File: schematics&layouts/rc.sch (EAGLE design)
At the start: 17 parts, among them IC1 L293D, IC2 L293D, Q1 16MHz, U1 ATMEGA328P-PU

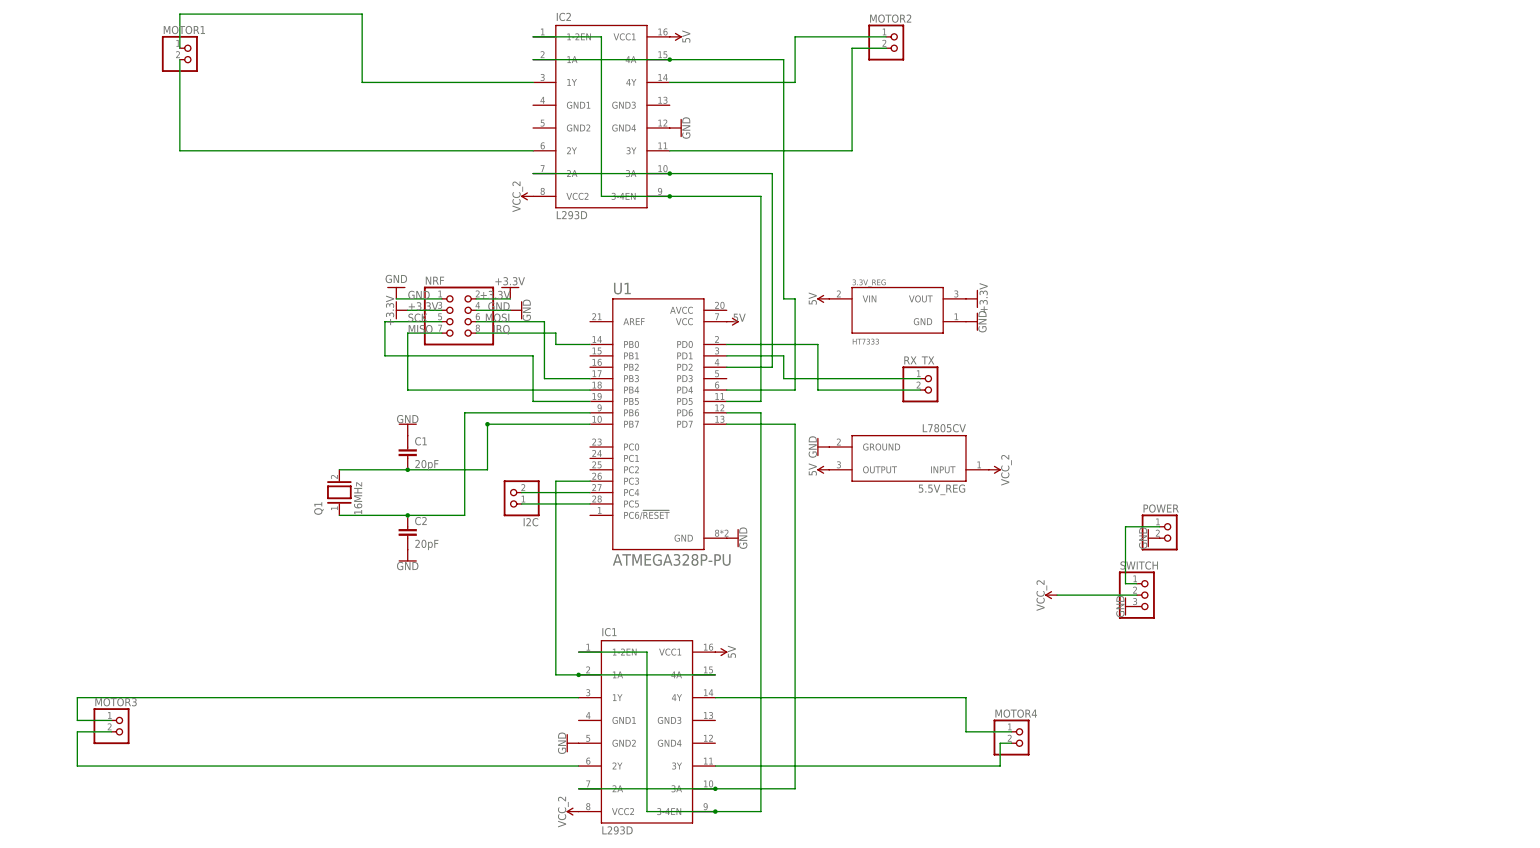
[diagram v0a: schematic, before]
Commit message: update schematic
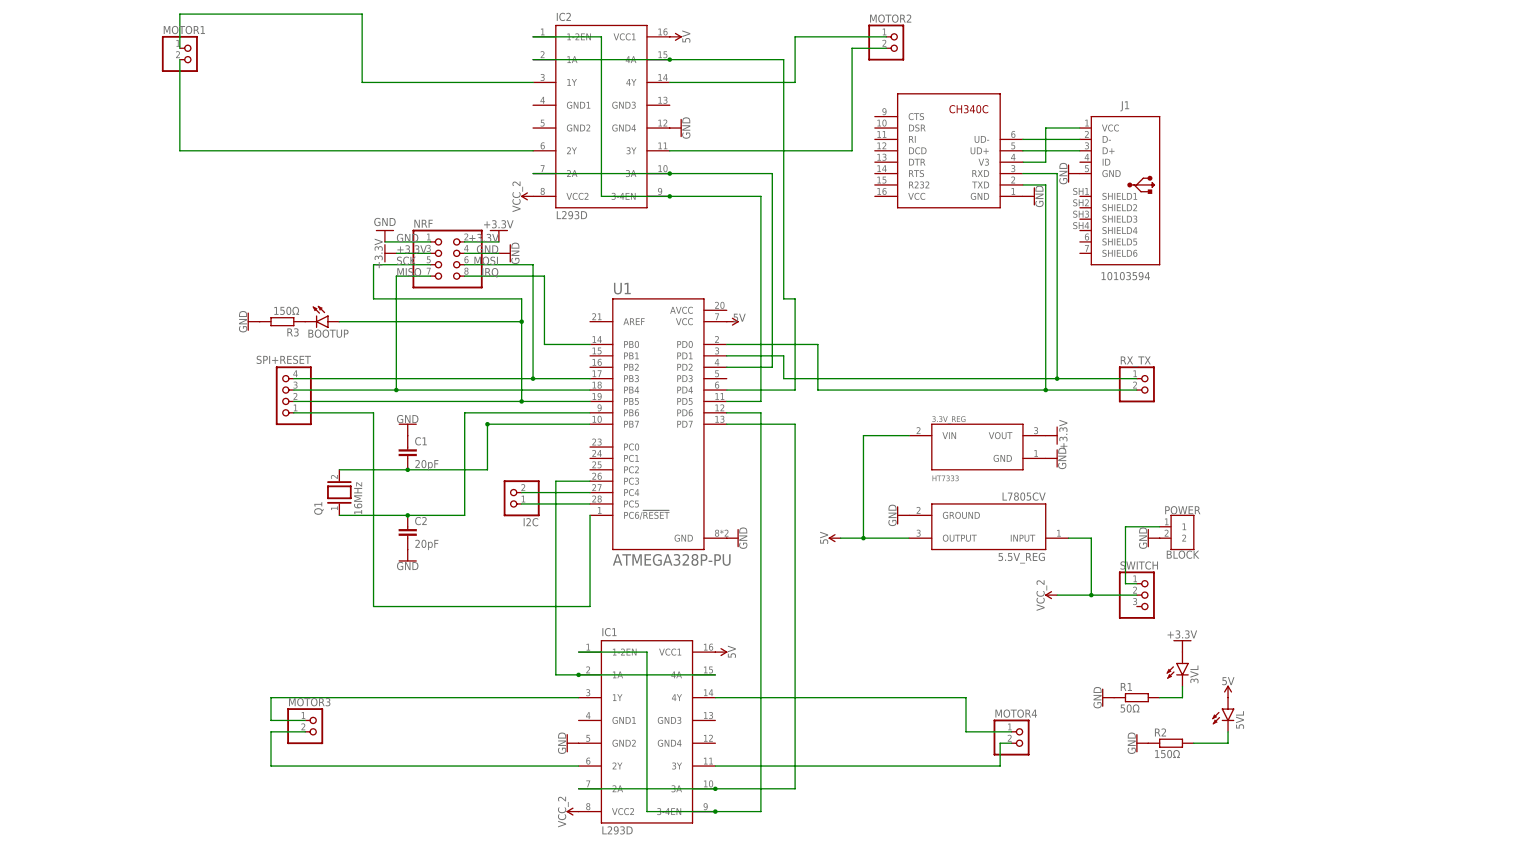
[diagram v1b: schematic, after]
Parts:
- added 3VL, 5VL, BOOTUP: (no value), led:LED5MM
- added J1: 10103594, Connector_USB:10103594
- added JP1: SPI+RESET, pinhead:PINHD-1X4
- added R1: 50Ω, rcl:R-EU_0204/7
- added R2, R3: 150Ω, rcl:R-EU_0204/7
- added U$1: CH340C, CH340C:CH340C
- POWER: value (none) -> BLOCK; device pinhead:PINHD-1X2 -> Connector:2828XX-2282834-2
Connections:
- new net N$22: 5VL.C, R2.2
- new net N$23: 3VL.C, R1.2
- new net N$24: J1.D-, U$1.UD-
- new net N$25: JP1.1, U1.PC6/!RESET
- new net N$26: J1.D+, U$1.UD+
- new net N$29: J1.VCC, U$1.V3
- net +3.3V: now also 3VL.A
- net 5V: now also 5VL.A
- net GND: now also BOOTUP.C, J1.GND, R1.1, R2.1, R3.1, R3.2, U$1.GND; no longer SWITCH.3
- net MISO: now also JP1.3
- net MOSI: now also JP1.4
- net N$18: now also U$1.TXD
- net N$2: now also U$1.RXD
- net SCK: now also BOOTUP.A, JP1.2
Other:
- moved on the sheet: 3.3V_REG, 5.5V_REG, MOTOR3, NRF, POWER, RX_TX

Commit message: updated schm
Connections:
- net N$7: now also MOTOR1.2; no longer MOTOR1.1
- net N$8: now also MOTOR1.1; no longer MOTOR1.2
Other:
- moved on the sheet: J1, MOTOR1, MOTOR2, RX_TX
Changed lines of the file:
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@@
 <attribute name="VALUE" x="56.134" y="111.76" size="1.778" layer="96" font="vector" rot="R90" align="top-center"/>
 </instance>
-<instance part="RX_TX" gate="G$1" x="198.12" y="81.28" smashed="yes">
-<attribute name="NAME" x="191.77" y="86.995" size="1.778" layer="95"/>
-<attribute name="VALUE" x="191.77" y="76.2" size="1.778" layer="96"/>
+<instance part="RX_TX" gate="G$1" x="226.06" y="91.44" smashed="yes" rot="R180">
+<attribute name="NAME" x="232.41" y="98.425" size="1.778" layer="95" rot="R180"/>
+<attribute name="VALUE" x="232.41" y="96.52" size="1.778" layer="96" rot="R180"/>
 </instance>
 <instance part="I2C" gate="G$1" x="55.88" y="58.42" smashed="yes" rot="R180">
@@
 <attribute name="VALUE" x="106.934" y="48.26" size="1.778" layer="96" font="vector" rot="R90" align="top-center"/>
 </instance>
-<instance part="MOTOR2" gate="G$1" x="142.24" y="157.48" smashed="yes">
-<attribute name="NAME" x="135.89" y="163.195" size="1.778" layer="95"/>
-<attribute name="VALUE" x="135.89" y="152.4" size="1.778" layer="96"/>
-</instance>
-<instance part="MOTOR1" gate="G$1" x="-15.24" y="154.94" smashed="yes">
-<attribute name="NAME" x="-21.59" y="160.655" size="1.778" layer="95"/>
-<attribute name="VALUE" x="-21.59" y="149.86" size="1.778" layer="96"/>
+<instance part="MOTOR2" gate="G$1" x="152.4" y="142.24" smashed="yes">
+<attribute name="NAME" x="146.05" y="147.955" size="1.778" layer="95"/>
+<attribute name="VALUE" x="146.05" y="137.16" size="1.778" layer="96"/>
+</instance>
+<instance part="MOTOR1" gate="G$1" x="-12.7" y="144.78" smashed="yes" rot="R180">
+<attribute name="NAME" x="-6.35" y="139.065" size="1.778" layer="95" rot="R180"/>
+<attribute name="VALUE" x="-6.35" y="149.86" size="1.778" layer="96" rot="R180"/>
 </instance>
 <instance part="SUPPLY5" gate="G$1" x="91.44" y="160.02" smashed="yes" rot="R270">
@@
 <attribute name="VALUE" x="-2.794" y="96.52" size="1.778" layer="96" font="vector" rot="R270" align="top-center"/>
 </instance>
-<instance part="J1" gate="G$1" x="193.04" y="127" smashed="yes">
-<attribute name="NAME" x="193.04" y="144.78" size="1.778" layer="95" align="center"/>
-<attribute name="VALUE" x="193.04" y="106.68" size="1.778" layer="96" align="center"/>
-</instance>
-<instance part="GND15" gate="1" x="172.72" y="124.46" smashed="yes" rot="R90">
-<attribute name="VALUE" x="172.974" y="124.46" size="1.778" layer="96" font="vector" rot="R90" align="top-center"/>
-</instance>
-<instance part="GND16" gate="1" x="180.34" y="129.54" smashed="yes" rot="R270">
-<attribute name="VALUE" x="180.086" y="129.54" size="1.778" layer="96" font="vector" rot="R270" align="top-center"/>
+<instance part="J1" gate="G$1" x="228.6" y="129.54" smashed="yes">
+<attribute name="NAME" x="228.6" y="147.32" size="1.778" layer="95" align="center"/>
+<attribute name="VALUE" x="228.6" y="109.22" size="1.778" layer="96" align="center"/>
+</instance>
+<instance part="GND15" gate="1" x="208.28" y="127" smashed="yes" rot="R90">
+<attribute name="VALUE" x="208.534" y="127" size="1.778" layer="96" font="vector" rot="R90" align="top-center"/>
+</instance>
+<instance part="GND16" gate="1" x="215.9" y="132.08" smashed="yes" rot="R270">
+<attribute name="VALUE" x="215.646" y="132.08" size="1.778" layer="96" font="vector" rot="R270" align="top-center"/>
 </instance>
 <instance part="POWER" gate="G$1" x="205.74" y="48.26" smashed="yes">
@@
 <attribute name="NAME" x="205.74" y="53.594" size="1.778" layer="95" align="bottom-center"/>
 </instance>
-<instance part="U$1" gate="G$1" x="154.94" y="134.62" smashed="yes" rot="R180"/>
+<instance part="U$1" gate="G$1" x="190.5" y="137.16" smashed="yes" rot="R180"/>
 </instances>
 <busses>
@@
 <pinref part="IC2" gate="G$1" pin="1Y"/>
 <wire x1="60.96" y1="149.86" x2="22.86" y2="149.86" width="0.1524" layer="91"/>
-<wire x1="22.86" y1="149.86" x2="22.86" y2="165.1" width="0.1524" layer="91"/>
-<wire x1="22.86" y1="165.1" x2="-17.78" y2="165.1" width="0.1524" layer="91"/>
-<wire x1="-17.78" y1="165.1" x2="-17.78" y2="157.48" width="0.1524" layer="91"/>
+<pinref part="MOTOR1" gate="G$1" pin="2"/>
+<wire x1="-10.16" y1="144.78" x2="22.86" y2="144.78" width="0.1524" layer="91"/>
+<wire x1="22.86" y1="144.78" x2="22.86" y2="149.86" width="0.1524" layer="91"/>
+</segment>
+</net>
+<net name="N$8" class="0">
+<segment>
+<pinref part="IC2" gate="G$1" pin="2Y"/>
 <pinref part="MOTOR1" gate="G$1" pin="1"/>
-</segment>
-</net>
-<net name="N$8" class="0">
-<segment>
-<pinref part="IC2" gate="G$1" pin="2Y"/>
-<wire x1="-17.78" y1="154.94" x2="-17.78" y2="134.62" width="0.1524" layer="91"/>
-<wire x1="-17.78" y1="134.62" x2="60.96" y2="134.62" width="0.1524" layer="91"/>
-<pinref part="MOTOR1" gate="G$1" pin="2"/>
+<wire x1="22.86" y1="134.62" x2="60.96" y2="134.62" width="0.1524" layer="91"/>
+<wire x1="-10.16" y1="142.24" x2="22.86" y2="142.24" width="0.1524" layer="91"/>
+<wire x1="22.86" y1="142.24" x2="22.86" y2="134.62" width="0.1524" layer="91"/>
 </segment>
 </net>
@@
 <pinref part="IC2" gate="G$1" pin="4Y"/>
 <wire x1="91.44" y1="149.86" x2="119.38" y2="149.86" width="0.1524" layer="91"/>
-<wire x1="119.38" y1="149.86" x2="119.38" y2="160.02" width="0.1524" layer="91"/>
-<wire x1="119.38" y1="160.02" x2="139.7" y2="160.02" width="0.1524" layer="91"/>
+<wire x1="119.38" y1="149.86" x2="119.38" y2="144.78" width="0.1524" layer="91"/>
+<wire x1="119.38" y1="144.78" x2="149.86" y2="144.78" width="0.1524" layer="91"/>
 <pinref part="MOTOR2" gate="G$1" pin="1"/>
 </segment>
@@
 <segment>
 <pinref part="IC2" gate="G$1" pin="3Y"/>
-<wire x1="91.44" y1="134.62" x2="132.08" y2="134.62" width="0.1524" layer="91"/>
-<wire x1="132.08" y1="134.62" x2="132.08" y2="157.48" width="0.1524" layer="91"/>
-<wire x1="132.08" y1="157.48" x2="139.7" y2="157.48" width="0.1524" layer="91"/>
+<wire x1="91.44" y1="134.62" x2="119.38" y2="134.62" width="0.1524" layer="91"/>
+<wire x1="119.38" y1="134.62" x2="119.38" y2="142.24" width="0.1524" layer="91"/>
+<wire x1="119.38" y1="142.24" x2="149.86" y2="142.24" width="0.1524" layer="91"/>
 <pinref part="MOTOR2" gate="G$1" pin="2"/>
 </segment>
@@
 <segment>
 <pinref part="U1" gate="G$1" pin="PD1"/>
-<wire x1="104.14" y1="88.9" x2="116.84" y2="88.9" width="0.1524" layer="91"/>
 <pinref part="RX_TX" gate="G$1" pin="1"/>
-<wire x1="116.84" y1="88.9" x2="116.84" y2="83.82" width="0.1524" layer="91"/>
-<wire x1="116.84" y1="83.82" x2="177.8" y2="83.82" width="0.1524" layer="91"/>
-<wire x1="177.8" y1="83.82" x2="195.58" y2="83.82" width="0.1524" layer="91"/>
-<wire x1="170.18" y1="129.54" x2="177.8" y2="129.54" width="0.1524" layer="91"/>
-<wire x1="177.8" y1="129.54" x2="177.8" y2="83.82" width="0.1524" layer="91"/>
-<junction x="177.8" y="83.82"/>
+<wire x1="104.14" y1="88.9" x2="213.36" y2="88.9" width="0.1524" layer="91"/>
+<wire x1="213.36" y1="88.9" x2="228.6" y2="88.9" width="0.1524" layer="91"/>
+<wire x1="205.74" y1="132.08" x2="213.36" y2="132.08" width="0.1524" layer="91"/>
+<wire x1="213.36" y1="132.08" x2="213.36" y2="88.9" width="0.1524" layer="91"/>
+<junction x="213.36" y="88.9"/>
 <pinref part="U$1" gate="G$1" pin="RXD"/>
 </segment>
@@
 <segment>
 <pinref part="U1" gate="G$1" pin="PD0"/>
-<wire x1="104.14" y1="91.44" x2="124.46" y2="91.44" width="0.1524" layer="91"/>
-<wire x1="124.46" y1="91.44" x2="124.46" y2="81.28" width="0.1524" layer="91"/>
 <pinref part="RX_TX" gate="G$1" pin="2"/>
-<wire x1="124.46" y1="81.28" x2="175.26" y2="81.28" width="0.1524" layer="91"/>
-<wire x1="175.26" y1="81.28" x2="195.58" y2="81.28" width="0.1524" layer="91"/>
-<wire x1="170.18" y1="127" x2="175.26" y2="127" width="0.1524" layer="91"/>
-<wire x1="175.26" y1="127" x2="175.26" y2="81.28" width="0.1524" layer="91"/>
-<junction x="175.26" y="81.28"/>
+<wire x1="104.14" y1="91.44" x2="210.82" y2="91.44" width="0.1524" layer="91"/>
+<wire x1="210.82" y1="91.44" x2="228.6" y2="91.44" width="0.1524" layer="91"/>
+<wire x1="205.74" y1="129.54" x2="210.82" y2="129.54" width="0.1524" layer="91"/>
+<wire x1="210.82" y1="129.54" x2="210.82" y2="91.44" width="0.1524" layer="91"/>
+<junction x="210.82" y="91.44"/>
 <pinref part="U$1" gate="G$1" pin="TXD"/>
 </segment>
@@
 <pinref part="J1" gate="G$1" pin="VCC"/>
 <pinref part="U$1" gate="G$1" pin="V3"/>
-<wire x1="175.26" y1="139.7" x2="182.88" y2="139.7" width="0.1524" layer="91"/>
-<wire x1="170.18" y1="132.08" x2="175.26" y2="132.08" width="0.1524" layer="91"/>
-<wire x1="175.26" y1="132.08" x2="175.26" y2="139.7" width="0.1524" layer="91"/>
+<wire x1="210.82" y1="142.24" x2="218.44" y2="142.24" width="0.1524" layer="91"/>
+<wire x1="205.74" y1="134.62" x2="210.82" y2="134.62" width="0.1524" layer="91"/>
+<wire x1="210.82" y1="134.62" x2="210.82" y2="142.24" width="0.1524" layer="91"/>
 </segment>
 </net>
@@
 <pinref part="U$1" gate="G$1" pin="UD-"/>
 <pinref part="J1" gate="G$1" pin="D-"/>
-<wire x1="170.18" y1="137.16" x2="182.88" y2="137.16" width="0.1524" layer="91"/>
+<wire x1="205.74" y1="139.7" x2="218.44" y2="139.7" width="0.1524" layer="91"/>
 </segment>
 </net>
@@
 <pinref part="U$1" gate="G$1" pin="UD+"/>
 <pinref part="J1" gate="G$1" pin="D+"/>
-<wire x1="170.18" y1="134.62" x2="182.88" y2="134.62" width="0.1524" layer="91"/>
-</segment>
-</net>
+<wire x1="205.74" y1="137.16" x2="218.44" y2="137.16" width="0.1524" layer="91"/>
+</segment>
+</net>

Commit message: Updated
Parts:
- removed 3.3V_REG: HT7333, HT7333:HT7333
- removed SWITCH: (no value), pinhead:PINHD-1X3
- added SWITCH-VCC: DS02E, Switch:DS02E
- added U2: LM1117T-3.3, LM1117T-3.3:LM1117T-3.3
- MOTOR1: value (none) -> AYE AM WALKIN' HERE
- MOTOR2: value (none) -> YO BOI GED
- renumbered RX_TX to TX_RX
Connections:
- net N$18 renamed RX
- net N$2 renamed TX
- new net N$27: POWER.1, SWITCH-VCC-2.1
- new net N$28: SWITCH-VCC-1.2, U1.VCC
- new net N$31: J1.GND, U$1.GND
- new net N$32: IC1.4A, U1.PD3
- new net N$33: IC1.2A, U1.PC2
- new net N$34: IC2.2A, U1.PB1
- new net N$35: IC2.1A, U1.PB2
- net +3.3V: now also U2.OUT; no longer 3.3V_REG.VOUT
- net 5V: now also SWITCH-VCC-1.1, U2.IN; no longer 3.3V_REG.VIN, U1.VCC
- net GND: now also IC1.GND4, U2.ADJ/GND; no longer 3.3V_REG.GND, IC1.GND2, J1.GND, R3.1, R3.2, U$1.GND
- net N$12: no longer IC2.1A
- net N$14: no longer IC2.2A
- net N$15: no longer IC1.2A
- net N$16: no longer IC1.4A
- net N$21: now also BOOTUP.A, R3.2; no longer POWER.1, SWITCH.1
- net SCK: now also R3.1; no longer BOOTUP.A
- net VCC_2: now also SWITCH-VCC-2.2; no longer SWITCH.2
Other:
- moved on the sheet: 3VL, 5VL, BOOTUP, C1, C2, I2C, NRF, POWER, Q1, R1, R2, R3

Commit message: updated enviroment configuration for usbasp
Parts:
- removed BOOTUP: (no value), led:LED5MM
- removed JP1: SPI+RESET, pinhead:PINHD-1X4
- removed R3: 150Ω, rcl:R-EU_0204/7
- added 3VTP, 5VTP, GNDTP, VCC2TP: TPB1,27, testpad:TPB1,27
- added PROGRAM_ME: ICSP, pinhead:PINHD-2X3
- MOTOR1: value AYE AM WALKIN' HERE -> B2B-XH-A; device pinhead:PINHD-1X2 -> Connector:B2B-XH-A
- MOTOR2: value YO BOI GED -> B2B-XH-A; device pinhead:PINHD-1X2 -> Connector:B2B-XH-A
- MOTOR3, MOTOR4: value (none) -> B2B-XH-A; device pinhead:PINHD-1X2 -> Connector:B2B-XH-A
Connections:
- removed net N$21: BOOTUP.A, R3.2
- removed net N$25: JP1.1, U1.PC6/!RESET
- new net RESET: PROGRAM_ME.5, U1.PC6/!RESET
- net +3.3V: now also 3VTP.TP
- net 5V: now also 5VTP.TP, PROGRAM_ME.2
- net GND: now also GNDTP.TP, PROGRAM_ME.6; no longer BOOTUP.C
- net MISO: now also PROGRAM_ME.1; no longer JP1.3
- net MOSI: now also PROGRAM_ME.4; no longer JP1.4
- net N$28: now also U$1.VCC
- net N$3: now also MOTOR3.1; no longer MOTOR4.1
- net N$4: now also MOTOR3.2; no longer MOTOR4.2
- net N$5: now also MOTOR4.1; no longer MOTOR3.1
- net N$6: now also MOTOR4.2; no longer MOTOR3.2
- net SCK: now also PROGRAM_ME.3; no longer JP1.2, R3.1
- net VCC_2: now also VCC2TP.TP
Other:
- moved on the sheet: MOTOR1, MOTOR2, MOTOR3, MOTOR4

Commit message: updated schematic
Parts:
- removed 3VTP, 5VTP, GNDTP, VCC2TP: TPB1,27, testpad:TPB1,27
- removed PROGRAM_ME: ICSP, pinhead:PINHD-2X3
- added ICSP: (no value), pinhead:PINHD-2X5
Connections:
- removed net N$29: J1.VCC, U$1.V3
- new net N$2: J1.VCC, U$1.VCC
- net +3.3V: no longer 3VTP.TP
- net 5V: now also ICSP.6; no longer 5VTP.TP, PROGRAM_ME.2
- net GND: now also ICSP.10; no longer GNDTP.TP, PROGRAM_ME.6
- net MISO: now also ICSP.5; no longer PROGRAM_ME.1
- net MOSI: now also ICSP.8; no longer PROGRAM_ME.4
- net N$28: no longer U$1.VCC
- net RESET: now also ICSP.9; no longer PROGRAM_ME.5
- net SCK: now also ICSP.7; no longer PROGRAM_ME.3
- net VCC_2: no longer VCC2TP.TP
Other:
- note added: "CHECK WITH USBasp Wiring"
